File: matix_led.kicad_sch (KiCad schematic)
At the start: 92 parts, among them U5 SN74LV1T34DCKR

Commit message: added footprints to compontents
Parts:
- R8: footprint (none) -> Capacitor_SMD:C_0402_1005Metric
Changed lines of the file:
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@@
     (property "Reference" "R8" (id 0) (at 48.895 147.955 90))
     (property "Value" "100k" (id 1) (at 48.895 150.495 90))
-    (property "Footprint" "" (id 2) (at 48.895 145.415 0)
+    (property "Footprint" "Capacitor_SMD:C_0402_1005Metric" (id 2) (at 48.895 145.415 0)
       (effects (font (size 1.27 1.27)) hide)
     )

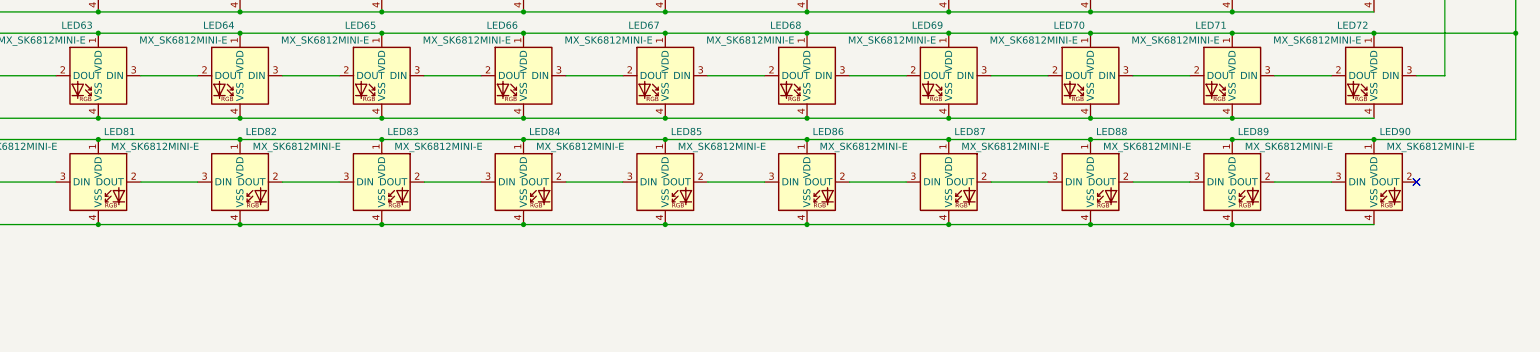
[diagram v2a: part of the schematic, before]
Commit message: placed switches and LEDs
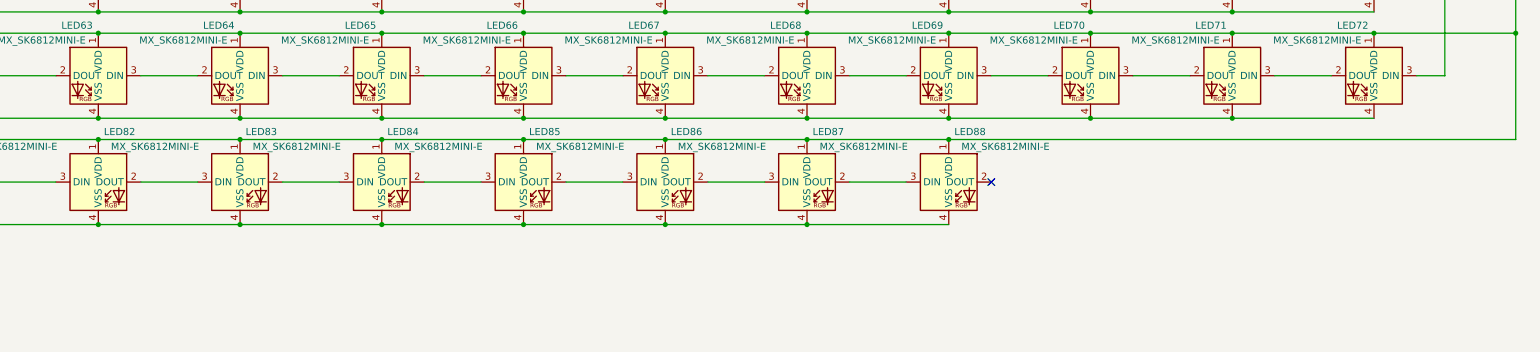
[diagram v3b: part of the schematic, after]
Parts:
- removed LED88, LED89, LED90: MX_SK6812MINI-E, marbastlib-mx:LED_MX_6028R, symbol marbastlib-mx:MX_SK6812MINI-E
- renumbered LED81 to LED82, LED82 to LED83, LED83 to LED84, LED84 to LED85, LED85 to LED86, LED86 to LED87, LED87 to LED88
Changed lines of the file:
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@@
   (junction (at 243.84 66.675) (diameter 0) (color 0 0 0 0)
   )
-  (junction (at 421.64 123.825) (diameter 0) (color 0 0 0 0)
-  )
   (junction (at 193.04 108.585) (diameter 0) (color 0 0 0 0)
   )
@@
   (junction (at 320.04 108.585) (diameter 0) (color 0 0 0 0)
   )
-  (junction (at 472.44 108.585) (diameter 0) (color 0 0 0 0)
-  )
   (junction (at 396.24 89.535) (diameter 0) (color 0 0 0 0)
   )
@@
   (junction (at 167.64 32.385) (diameter 0) (color 0 0 0 0)
   )
-  (junction (at 447.04 108.585) (diameter 0) (color 0 0 0 0)
-  )
   (junction (at 269.24 47.625) (diameter 0) (color 0 0 0 0)
   )
@@
   (junction (at 345.44 51.435) (diameter 0) (color 0 0 0 0)
   )
-  (junction (at 421.64 108.585) (diameter 0) (color 0 0 0 0)
-  )
   (junction (at 447.04 47.625) (diameter 0) (color 0 0 0 0)
   )
@@
   (junction (at 294.64 89.535) (diameter 0) (color 0 0 0 0)
   )
-  (junction (at 447.04 123.825) (diameter 0) (color 0 0 0 0)
-  )
   (junction (at 345.44 123.825) (diameter 0) (color 0 0 0 0)
   )
@@
   (junction (at 472.44 51.435) (diameter 0) (color 0 0 0 0)
   )
-  (junction (at 396.24 123.825) (diameter 0) (color 0 0 0 0)
-  )
   (junction (at 66.04 89.535) (diameter 0) (color 0 0 0 0)
   )
@@
   (junction (at 91.44 51.435) (diameter 0) (color 0 0 0 0)
   )
-  (no_connect (at 480.06 116.205))
+  (no_connect (at 403.86 116.205))
   (wire (pts (xy 142.24 108.585) (xy 116.84 108.585))
     (stroke (width 0) (type default) (color 0 0 0 0))
@@
     (stroke (width 0) (type default) (color 0 0 0 0))
   )
-  (wire (pts (xy 454.66 116.205) (xy 464.82 116.205))
-    (stroke (width 0) (type default) (color 0 0 0 0))
-  )
   (wire (pts (xy 175.26 97.155) (xy 185.42 97.155))
     (stroke (width 0) (type default) (color 0 0 0 0))
@@
     (stroke (width 0) (type default) (color 0 0 0 0))
   )
-  (wire (pts (xy 403.86 116.205) (xy 414.02 116.205))
-    (stroke (width 0) (type default) (color 0 0 0 0))
-  )
   (wire (pts (xy 124.46 78.105) (xy 134.62 78.105))
     (stroke (width 0) (type default) (color 0 0 0 0))
@@
     (stroke (width 0) (type default) (color 0 0 0 0))
   )
-  (wire (pts (xy 421.64 108.585) (xy 396.24 108.585))
+  (wire (pts (xy 396.24 108.585) (xy 497.84 108.585))
     (stroke (width 0) (type default) (color 0 0 0 0))
   )
@@
     (stroke (width 0) (type default) (color 0 0 0 0))
   )
-  (wire (pts (xy 497.84 108.585) (xy 472.44 108.585))
-    (stroke (width 0) (type default) (color 0 0 0 0))
-  )
   (wire (pts (xy 251.46 78.105) (xy 261.62 78.105))
     (stroke (width 0) (type default) (color 0 0 0 0))
@@
     (stroke (width 0) (type default) (color 0 0 0 0))
   )
-  (wire (pts (xy 472.44 123.825) (xy 447.04 123.825))
-    (stroke (width 0) (type default) (color 0 0 0 0))
-  )
   (wire (pts (xy 193.04 70.485) (xy 218.44 70.485))
     (stroke (width 0) (type default) (color 0 0 0 0))
@@
     (stroke (width 0) (type default) (color 0 0 0 0))
   )
-  (wire (pts (xy 447.04 123.825) (xy 421.64 123.825))
-    (stroke (width 0) (type default) (color 0 0 0 0))
-  )
   (wire (pts (xy 193.04 108.585) (xy 167.64 108.585))
     (stroke (width 0) (type default) (color 0 0 0 0))
@@
     (stroke (width 0) (type default) (color 0 0 0 0))
   )
-  (wire (pts (xy 472.44 108.585) (xy 447.04 108.585))
-    (stroke (width 0) (type default) (color 0 0 0 0))
-  )
   (wire (pts (xy 302.26 59.055) (xy 312.42 59.055))
     (stroke (width 0) (type default) (color 0 0 0 0))
@@
     (stroke (width 0) (type default) (color 0 0 0 0))
   )
-  (wire (pts (xy 421.64 123.825) (xy 396.24 123.825))
-    (stroke (width 0) (type default) (color 0 0 0 0))
-  )
   (wire (pts (xy 73.66 116.205) (xy 83.82 116.205))
     (stroke (width 0) (type default) (color 0 0 0 0))
@@
     (stroke (width 0) (type default) (color 0 0 0 0))
   )
-  (wire (pts (xy 429.26 116.205) (xy 439.42 116.205))
-    (stroke (width 0) (type default) (color 0 0 0 0))
-  )
   (wire (pts (xy 200.66 78.105) (xy 210.82 78.105))
     (stroke (width 0) (type default) (color 0 0 0 0))
@@
   )
   (wire (pts (xy 454.66 59.055) (xy 464.82 59.055))
-    (stroke (width 0) (type default) (color 0 0 0 0))
-  )
-  (wire (pts (xy 447.04 108.585) (xy 421.64 108.585))
     (stroke (width 0) (type default) (color 0 0 0 0))
   )
@@
   (symbol (lib_id "marbastlib-mx:MX_SK6812MINI-E") (at 294.64 116.205 0) (unit 1)
     (in_bom yes) (on_board yes)
-    (property "Reference" "LED83" (id 0) (at 298.45 107.2007 0))
+    (property "Reference" "LED84" (id 0) (at 298.45 107.2007 0))
     (property "Value" "MX_SK6812MINI-E" (id 1) (at 304.8 109.855 0))
     (property "Footprint" "marbastlib-mx:LED_MX_6028R" (id 2) (at 294.64 116.205 0)
@@
     (pin "4")
   )
-  (symbol (lib_id "marbastlib-mx:MX_SK6812MINI-E") (at 421.64 116.205 0) (unit 1)
-    (in_bom yes) (on_board yes)
-    (property "Reference" "LED88" (id 0) (at 425.45 107.2007 0))
-    (property "Value" "MX_SK6812MINI-E" (id 1) (at 431.8 109.855 0))
-    (property "Footprint" "marbastlib-mx:LED_MX_6028R" (id 2) (at 421.64 116.205 0)
-      (effects (font (size 1.27 1.27)) hide)
-    )
-    (property "Datasheet" "" (id 3) (at 421.64 116.205 0)
-      (effects (font (size 1.27 1.27)) hide)
-    )
-    (pin "1")
-    (pin "2")
-    (pin "3")
-    (pin "4")
-  )
   (symbol (lib_id "power:+5V") (at 497.84 27.305 0) (unit 1)
     (in_bom yes) (on_board yes) (fields_autoplaced)
@@
     (pin "4")
   )
-  (symbol (lib_id "marbastlib-mx:MX_SK6812MINI-E") (at 472.44 116.205 0) (unit 1)
-    (in_bom yes) (on_board yes)
-    (property "Reference" "LED90" (id 0) (at 476.25 107.2007 0))
-    (property "Value" "MX_SK6812MINI-E" (id 1) (at 482.6 109.855 0))
-    (property "Footprint" "marbastlib-mx:LED_MX_6028R" (id 2) (at 472.44 116.205 0)
-      (effects (font (size 1.27 1.27)) hide)
-    )
-    (property "Datasheet" "" (id 3) (at 472.44 116.205 0)
-      (effects (font (size 1.27 1.27)) hide)
-    )
-    (pin "1")
-    (pin "2")
-    (pin "3")
-    (pin "4")
-  )
   (symbol (lib_id "marbastlib-mx:MX_SK6812MINI-E") (at 472.44 59.055 0) (mirror y) (unit 1)
     (in_bom yes) (on_board yes)
@@
   (symbol (lib_id "marbastlib-mx:MX_SK6812MINI-E") (at 345.44 116.205 0) (unit 1)
     (in_bom yes) (on_board yes)
-    (property "Reference" "LED85" (id 0) (at 349.25 107.2007 0))
+    (property "Reference" "LED86" (id 0) (at 349.25 107.2007 0))
     (property "Value" "MX_SK6812MINI-E" (id 1) (at 355.6 109.855 0))
     (property "Footprint" "marbastlib-mx:LED_MX_6028R" (id 2) (at 345.44 116.205 0)
@@
   (symbol (lib_id "marbastlib-mx:MX_SK6812MINI-E") (at 243.84 116.205 0) (unit 1)
     (in_bom yes) (on_board yes)
-    (property "Reference" "LED81" (id 0) (at 247.65 107.2007 0))
+    (property "Reference" "LED82" (id 0) (at 247.65 107.2007 0))
     (property "Value" "MX_SK6812MINI-E" (id 1) (at 254 109.855 0))
     (property "Footprint" "marbastlib-mx:LED_MX_6028R" (id 2) (at 243.84 116.205 0)
@@
     (pin "4")
   )
-  (symbol (lib_id "marbastlib-mx:MX_SK6812MINI-E") (at 447.04 116.205 0) (unit 1)
-    (in_bom yes) (on_board yes)
-    (property "Reference" "LED89" (id 0) (at 450.85 107.2007 0))
-    (property "Value" "MX_SK6812MINI-E" (id 1) (at 457.2 109.855 0))
-    (property "Footprint" "marbastlib-mx:LED_MX_6028R" (id 2) (at 447.04 116.205 0)
-      (effects (font (size 1.27 1.27)) hide)
-    )
-    (property "Datasheet" "" (id 3) (at 447.04 116.205 0)
-      (effects (font (size 1.27 1.27)) hide)
-    )
-    (pin "1")
-    (pin "2")
-    (pin "3")
-    (pin "4")
-  )
   (symbol (lib_id "marbastlib-mx:MX_SK6812MINI-E") (at 218.44 97.155 0) (mirror y) (unit 1)
     (in_bom yes) (on_board yes)
@@
   (symbol (lib_id "marbastlib-mx:MX_SK6812MINI-E") (at 320.04 116.205 0) (unit 1)
     (in_bom yes) (on_board yes)
-    (property "Reference" "LED84" (id 0) (at 323.85 107.2007 0))
+    (property "Reference" "LED85" (id 0) (at 323.85 107.2007 0))
     (property "Value" "MX_SK6812MINI-E" (id 1) (at 330.2 109.855 0))
     (property "Footprint" "marbastlib-mx:LED_MX_6028R" (id 2) (at 320.04 116.205 0)
@@
   (symbol (lib_id "marbastlib-mx:MX_SK6812MINI-E") (at 396.24 116.205 0) (unit 1)
     (in_bom yes) (on_board yes)
-    (property "Reference" "LED87" (id 0) (at 400.05 107.2007 0))
+    (property "Reference" "LED88" (id 0) (at 400.05 107.2007 0))
     (property "Value" "MX_SK6812MINI-E" (id 1) (at 406.4 109.855 0))
     (property "Footprint" "marbastlib-mx:LED_MX_6028R" (id 2) (at 396.24 116.205 0)
@@
   (symbol (lib_id "marbastlib-mx:MX_SK6812MINI-E") (at 269.24 116.205 0) (unit 1)
     (in_bom yes) (on_board yes)
-    (property "Reference" "LED82" (id 0) (at 273.05 107.2007 0))
+    (property "Reference" "LED83" (id 0) (at 273.05 107.2007 0))
     (property "Value" "MX_SK6812MINI-E" (id 1) (at 279.4 109.855 0))
     (property "Footprint" "marbastlib-mx:LED_MX_6028R" (id 2) (at 269.24 116.205 0)
@@
   (symbol (lib_id "marbastlib-mx:MX_SK6812MINI-E") (at 370.84 116.205 0) (unit 1)
     (in_bom yes) (on_board yes)
-    (property "Reference" "LED86" (id 0) (at 374.65 107.2007 0))
+    (property "Reference" "LED87" (id 0) (at 374.65 107.2007 0))
     (property "Value" "MX_SK6812MINI-E" (id 1) (at 381 109.855 0))
     (property "Footprint" "marbastlib-mx:LED_MX_6028R" (id 2) (at 370.84 116.205 0)
